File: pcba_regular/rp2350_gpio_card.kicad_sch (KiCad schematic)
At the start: 38 parts, among them J1 Conn_01x10_Pin, J2 Conn_01x10_Pin, P1 USB_C_Plug_USB2.0, U1 RP2350_60QFN, U2 W25Q128JVS, U4 AP2127K-3.3, Y1 ABM8-272-T3

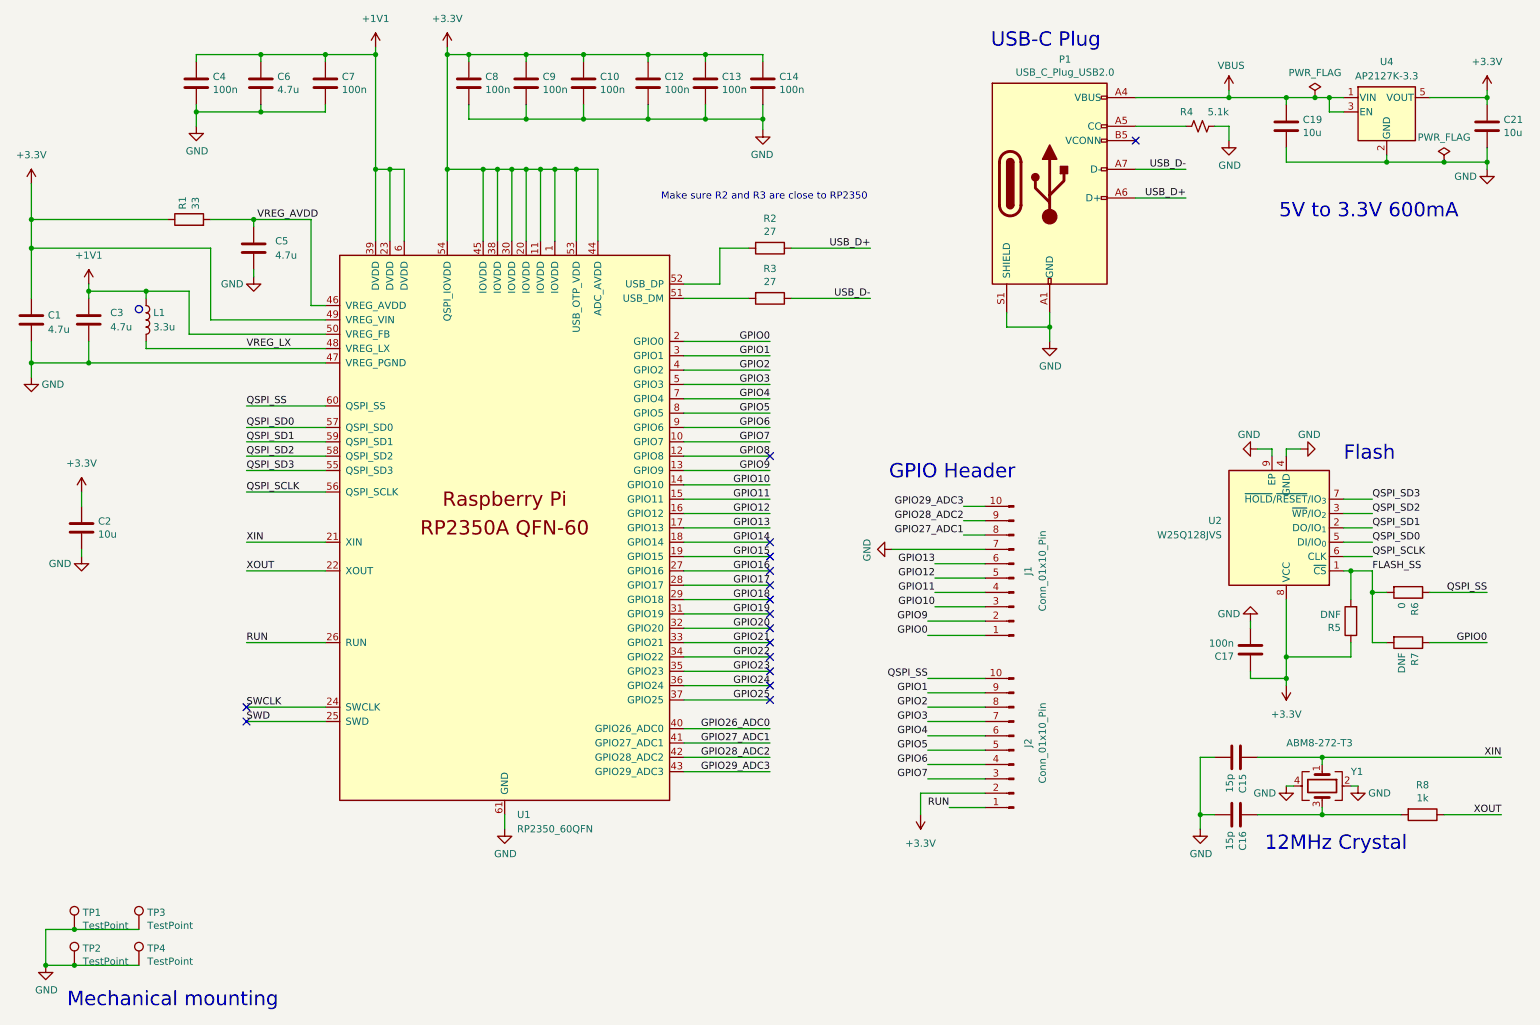
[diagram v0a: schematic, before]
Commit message: optimized PCB layout
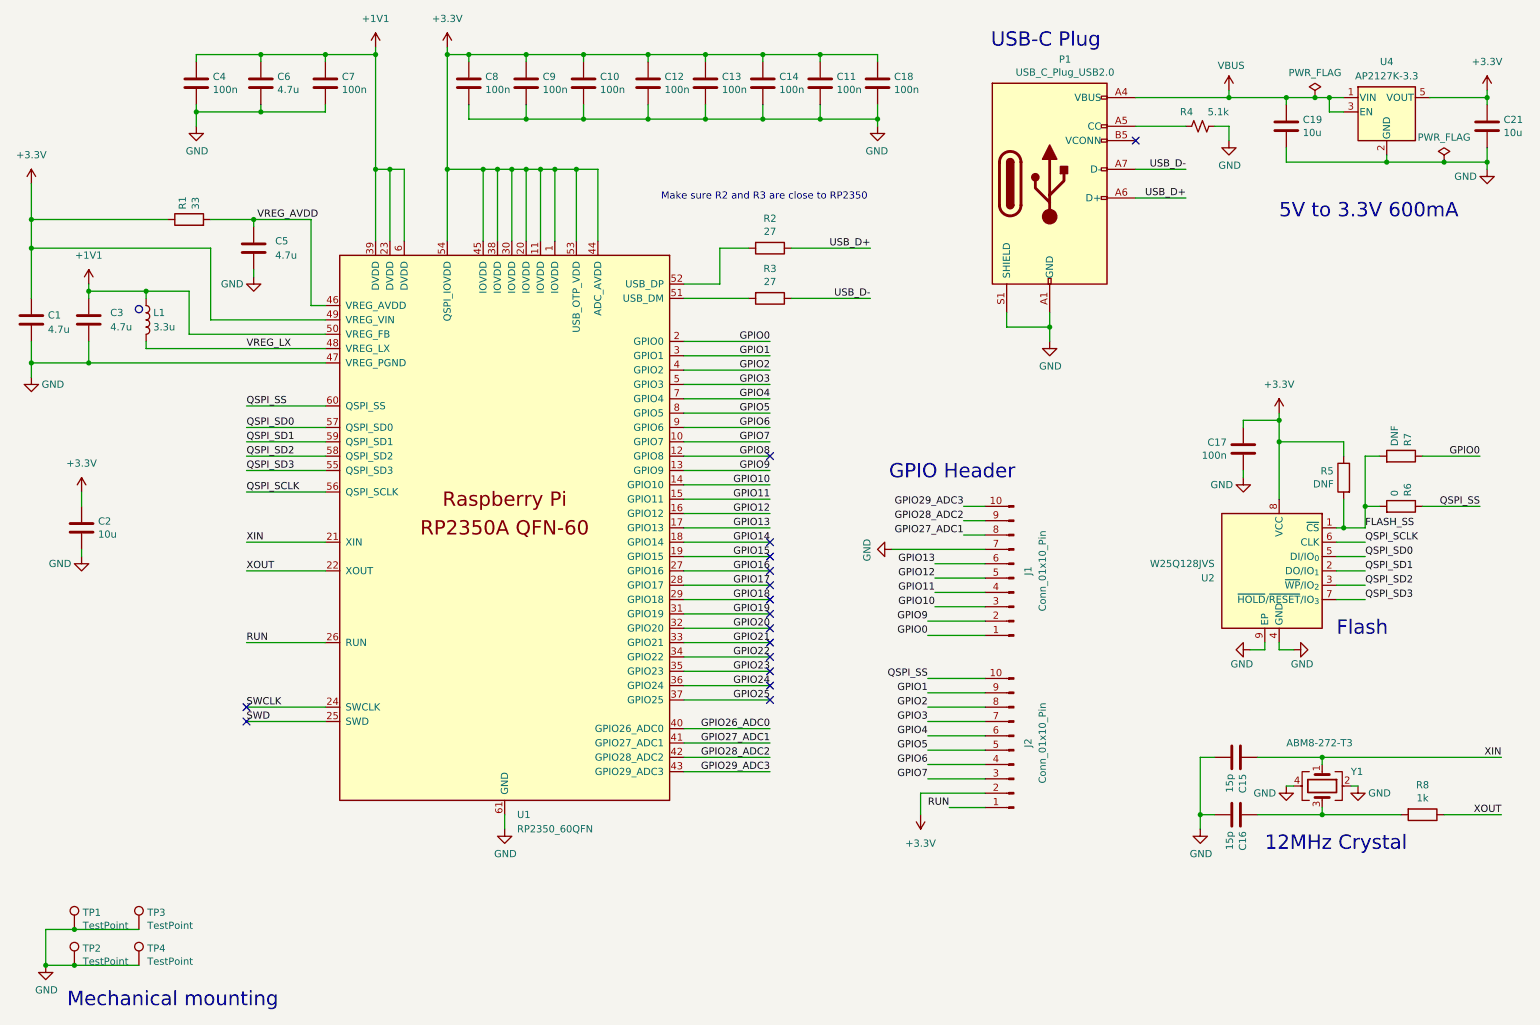
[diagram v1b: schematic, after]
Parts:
- added C11, C18: 100n, Capacitor_SMD:C_0402_1005Metric, symbol Device:C
- R4: footprint Resistor_SMD:R_0603_1608Metric -> Resistor_SMD:R_0402_1005Metric
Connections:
- net +3.3V: now also C11.1, C18.1
- net GND: now also C11.2, C18.2
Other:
- moved on the sheet: C17, R5, R6, R7, U2
